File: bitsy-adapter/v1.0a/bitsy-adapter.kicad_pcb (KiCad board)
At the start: 2 copper layers, 76 x 36 mm, 31 parts, among them J1 PMOD1, J2 PMOD2, J3 PMOD3, J4 5V AUX, J5 5V AUX

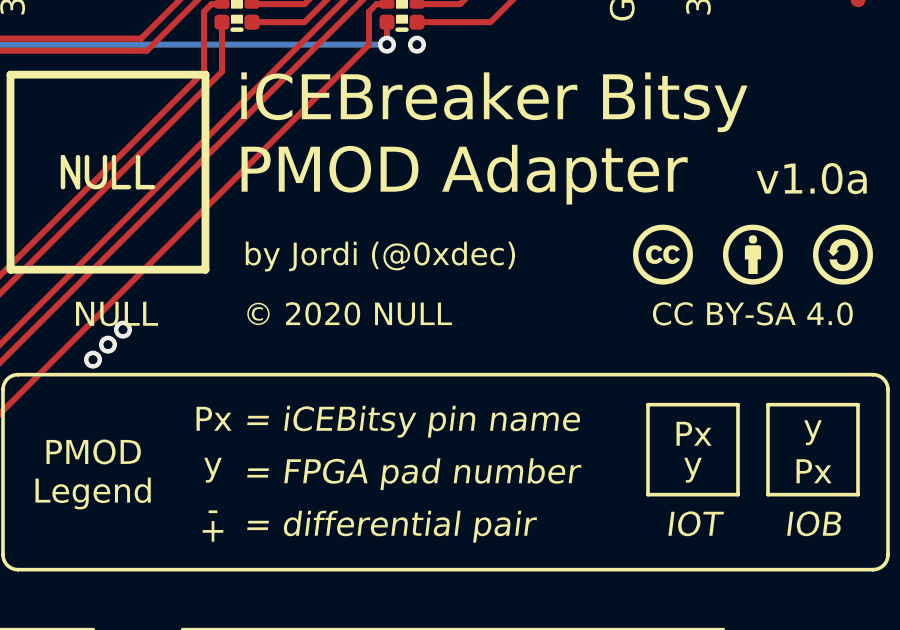
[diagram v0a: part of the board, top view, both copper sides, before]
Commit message: Bitsy Adapter: fix copyright
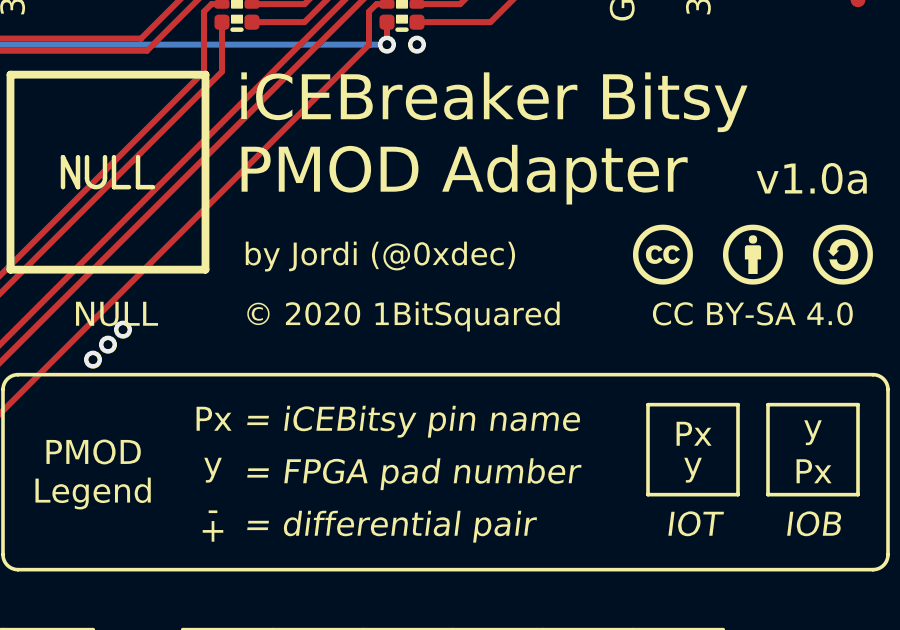
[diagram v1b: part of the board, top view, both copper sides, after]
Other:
- board text added: "© 2020 1BitSquared"
- board text removed: "© 2020 NULL"
